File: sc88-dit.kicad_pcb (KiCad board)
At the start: 2 copper layers, 70 x 51 mm, 72 parts, among them J1 Conn_01x04_Male, J2 Conn_01x04_Male, J3 Conn_01x06_Male, J4 Conn_01x06_Male, U1 74LVC1G74, U2 AK4103A

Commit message: Added an oppai-sauce logo
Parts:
- added G***: LOGO, components:opppaisauce, B.Cu at (34.2, 115.0)

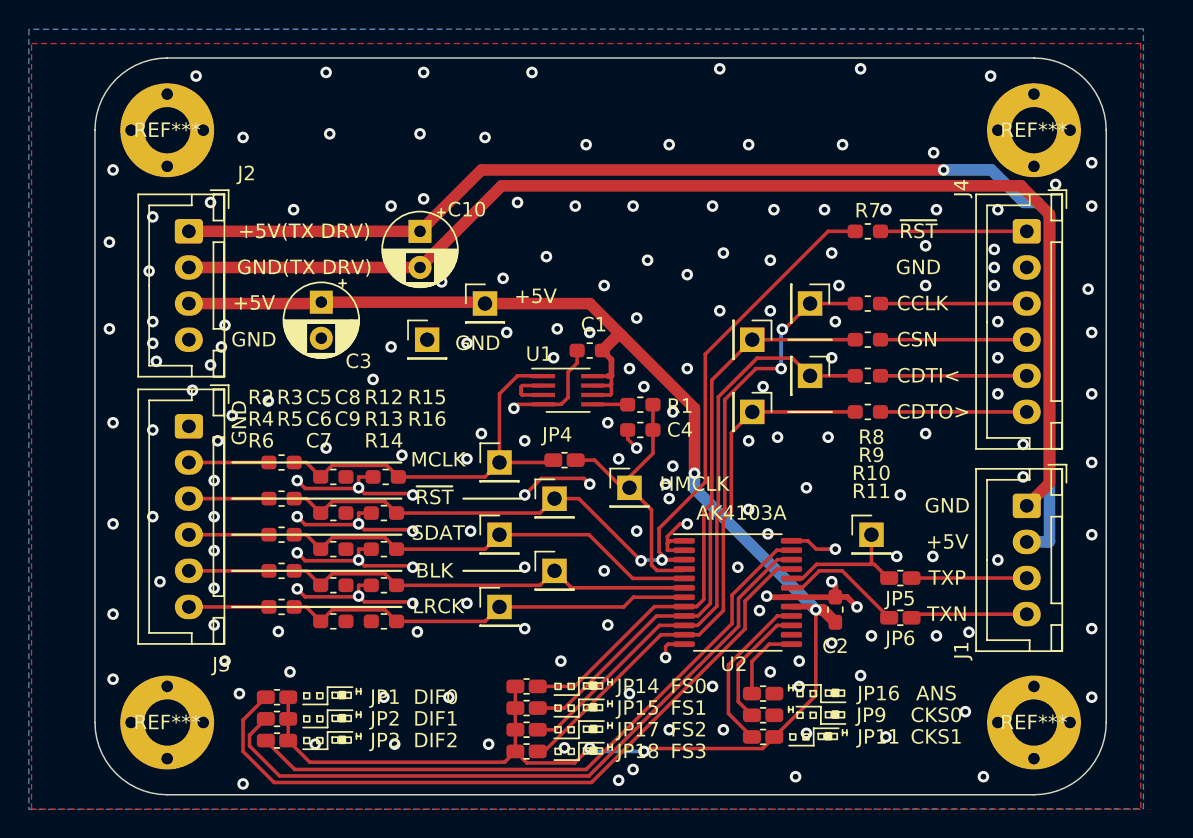
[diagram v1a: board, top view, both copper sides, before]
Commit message: To use right-angle connectors
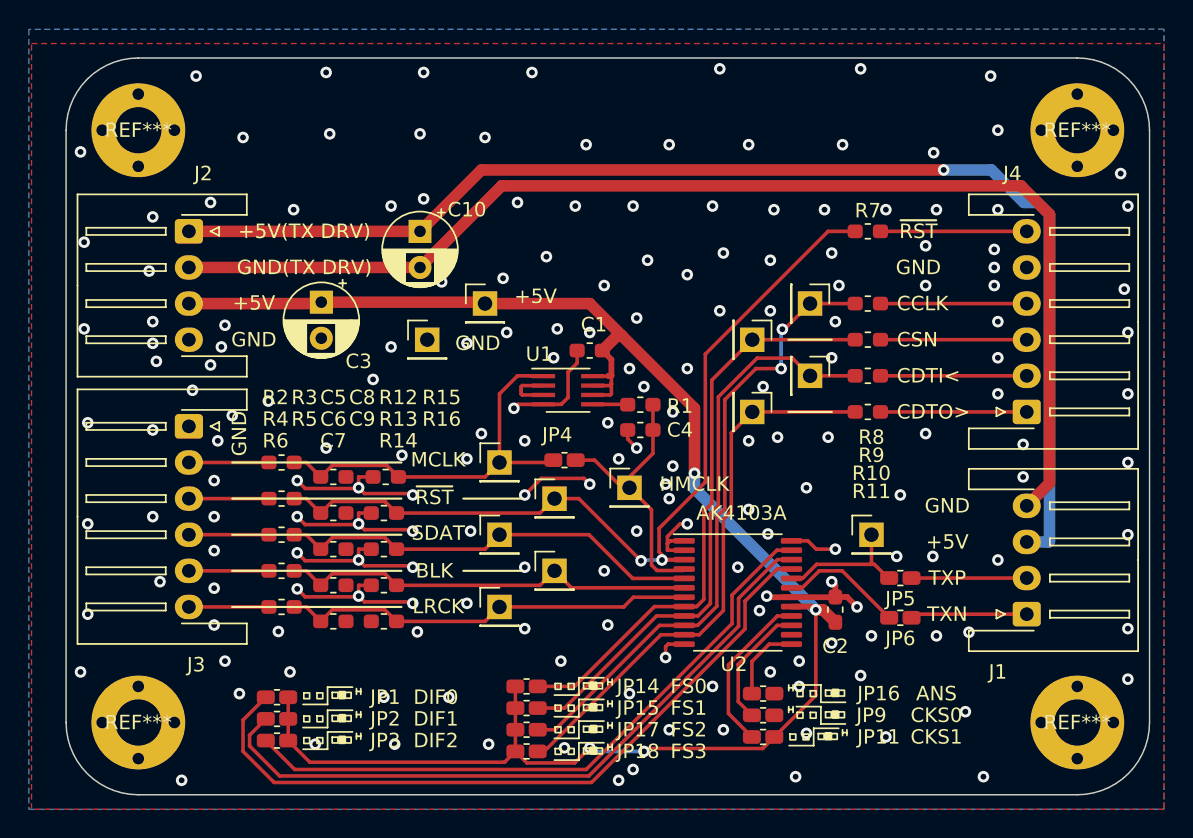
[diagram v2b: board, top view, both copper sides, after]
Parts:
- J1, J2: footprint Connector_JST:JST_XH_B4B-XH-A_1x04_P2.50mm_Vertical -> Connector_JST:JST_XH_S4B-XH-A-1_1x04_P2.50mm_Horizontal
- J3, J4: footprint Connector_JST:JST_XH_B6B-XH-A_1x06_P2.50mm_Vertical -> Connector_JST:JST_XH_S6B-XH-A-1_1x06_P2.50mm_Horizontal
- moved J4 12.5 mm to (81.5, 104.5), turned to 90 degrees
- moved J1 7.50 mm to (81.5, 118.5), turned to 90 degrees
- moved REF*** 3.00 mm to (85.0, 126.0)
- moved REF*** 3.00 mm to (85.0, 85.0)
- moved REF*** 2.00 mm to (20.0, 85.0)
- moved REF*** 2.00 mm to (20.0, 126.0)
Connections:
- J1 pad 1: /LEDK -> Net-(J1-Pad1)
- J1 pad 2: /LEDA -> Net-(J1-Pad2)
- J1 pad 3: Net-(J1-Pad3) -> /LEDA
- J1 pad 4: Net-(J1-Pad4) -> /LEDK
- J4 pad 2: GND -> Net-(J4-Pad2)
- J4 pad 5: Net-(J4-Pad5) -> GND
- JP5 pad 1: Net-(J1-Pad3) -> Net-(J1-Pad2)
- JP6 pad 1: Net-(J1-Pad4) -> Net-(J1-Pad1)
- R10 pad 2: Net-(J4-Pad5) -> Net-(J4-Pad2)
- R11 pad 2: Net-(J4-Pad6) -> Net-(J4-Pad1)
- R7 pad 2: Net-(J4-Pad1) -> Net-(J4-Pad6)
- R8 pad 2: Net-(J4-Pad3) -> Net-(J4-Pad4)
- R9 pad 2: Net-(J4-Pad4) -> Net-(J4-Pad3)
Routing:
- net Net-(J4-Pad5): track 10.1 -> 0.00 mm
- net Net-(J4-Pad2): track 0.00 -> 10.1 mm
- net Net-(J1-Pad4): track 8.08 -> 0.00 mm
- net Net-(J1-Pad1): track 0.00 -> 8.08 mm
- net Net-(J1-Pad3): track 7.97 -> 0.00 mm
- net Net-(J1-Pad2): track 0.00 -> 7.97 mm
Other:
- board size 70 x 51 mm -> 75 x 51 mm

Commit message: Refined VCC line
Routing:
- net +5V: track 123.1 -> 127.6 mm
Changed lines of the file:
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@@
   (general
     (thickness 1.6)
-    (drawings 51)
-    (tracks 517)
+    (drawings 52)
+    (tracks 521)
     (modules 73)
     (nets 37)
@@
     (tags "resistor handsolder")
     (attr smd)
-    (fp_text reference "R11" (at 0.25 5.5) (layer "F.SilkS")
+    (fp_text reference "R11" (at -0.15 3) (layer "F.SilkS")
       (effects (font (size 1 1) (thickness 0.15)))
     )
@@
     (tags "resistor handsolder")
     (attr smd)
-    (fp_text reference "R10" (at 0.25 6.75) (layer "F.SilkS")
+    (fp_text reference "R10" (at -0.15 4.15) (layer "F.SilkS")
       (effects (font (size 1 1) (thickness 0.15)))
     )
@@
     (tags "resistor handsolder")
     (attr smd)
-    (fp_text reference "R9" (at 0.25 8) (layer "F.SilkS")
+    (fp_text reference "R9" (at 0.05 -4.2) (layer "F.SilkS")
       (effects (font (size 1 1) (thickness 0.15)))
     )
@@
     (tags "resistor handsolder")
     (attr smd)
-    (fp_text reference "R8" (at 0.25 9.25) (layer "F.SilkS")
+    (fp_text reference "R8" (at 0.05 -3.3) (layer "F.SilkS")
       (effects (font (size 1 1) (thickness 0.15)))
     )
@@
     )
   )
+  (gr_text "TXP" (at 67.65 111.65) (layer "F.SilkS")
+    (effects (font (size 1 1) (thickness 0.15)))
+  )
   (gr_text "GND" (at 27 106 90) (layer "F.SilkS")
     (effects (font (size 1 1) (thickness 0.15)))
@@
     (effects (font (size 1 1) (thickness 0.15)))
   )
+  (via (at 67.7 121.6) (size 0.8) (drill 0.4) (layers "F.Cu" "B.Cu") (net 2))
+  (via (at 65.45 121.75) (size 0.8) (drill 0.4) (layers "F.Cu" "B.Cu") (net 2))
+  (segment (start 68.25032 119.44968) (end 66.55 121.15) (width 0.25) (layer "F.Cu") (net 3))
+  (segment (start 68.25032 119.058874) (end 68.25032 119.44968) (width 0.25) (layer "F.Cu") (net 3))
+  (segment (start 66.55 124.475) (end 64.025 127) (width 0.25) (layer "F.Cu") (net 3))
+  (segment (start 66.55 121.15) (end 66.55 124.475) (width 0.25) (layer "F.Cu") (net 3))
+  (segment (start 65.2125 117.975) (end 66.375 117.975) (width 0.4) (layer "F.Cu") (net 3))
+  (segment (start 66.375 117.975) (end 67.05 118.65) (width 0.4) (layer "F.Cu") (net 3))
+  (segment (start 67.05 118.65) (end 67.458874 119.058874) (width 0.4) (layer "F.Cu") (net 3))
+  (segment (start 67.458874 119.058874) (end 68.25032 119.058874) (width 0.4) (layer "F.Cu") (net 3))
+  (segment (start 67.2 119.1) (end 69.6 119.1) (width 0.8) (layer "B.Cu") (net 3))
+  (segment (start 69.558874 119.058874) (end 69.6 119.1) (width 0.8) (layer "F.Cu") (net 3))
+  (segment (start 68.25032 119.058874) (end 69.558874 119.058874) (width 0.8) (layer "F.Cu") (net 3))
+  (segment (start 58.5 110.4) (end 67.2 119.1) (width 0.8) (layer "B.Cu") (net 3))
+  (segment (start 58.5 108.75) (end 58.5 110.4) (width 0.8) (layer "B.Cu") (net 3))
+  (via (at 69.6 119.1) (size 0.8) (drill 0.4) (layers "F.Cu" "B.Cu") (net 3))
   (via (at 62.25 111.25) (size 0.8) (drill 0.4) (layers "F.Cu" "B.Cu") (net 2))
   (via (at 61.5 115.25) (size 0.8) (drill 0.4) (layers "F.Cu" "B.Cu") (net 2))
-  (segment (start 66.6 117.9) (end 66.9 118.2) (width 0.8) (layer "B.Cu") (net 3))
-  (segment (start 58.5 108.75) (end 58.5 109.8) (width 0.8) (layer "B.Cu") (net 3))
-  (segment (start 58.5 109.8) (end 66.6 117.9) (width 0.8) (layer "B.Cu") (net 3))
   (via (at 63.582059 112.945294) (size 0.8) (drill 0.4) (layers "F.Cu" "B.Cu") (net 2))
   (via (at 38.25 107.5) (size 0.8) (drill 0.4) (layers "F.Cu" "B.Cu") (net 2))
@@
   (segment (start 68.25032 116.50032) (end 68 116.25) (width 0.4) (layer "F.Cu") (net 2))
   (via (at 68 116.25) (size 0.8) (drill 0.4) (layers "F.Cu" "B.Cu") (net 2))
-  (via (at 68 120.5) (size 0.8) (drill 0.4) (layers "F.Cu" "B.Cu") (net 2))
   (segment (start 69.058874 117.308874) (end 69.75 118) (width 0.4) (layer "F.Cu") (net 2))
   (segment (start 65.2125 117.325) (end 68.234194 117.325) (width 0.4) (layer "F.Cu") (net 2))
   (segment (start 68.25032 117.308874) (end 69.058874 117.308874) (width 0.4) (layer "F.Cu") (net 2))
-  (segment (start 67.391446 118.2) (end 68.25032 119.058874) (width 0.8) (layer "F.Cu") (net 3))
-  (segment (start 66.9 118.2) (end 67.391446 118.2) (width 0.8) (layer "F.Cu") (net 3))
   (segment (start 68.234194 117.325) (end 68.25032 117.308874) (width 0.4) (layer "F.Cu") (net 2))
   (via (at 58 95) (size 0.8) (drill 0.4) (layers "F.Cu" "B.Cu") (net 2))
@@
   (via (at 59.75 123.5) (size 0.8) (drill 0.4) (layers "F.Cu" "B.Cu") (net 2))
   (via (at 65.75 123.5) (size 0.8) (drill 0.4) (layers "F.Cu" "B.Cu") (net 2))
-  (via (at 65.75 121.75) (size 0.8) (drill 0.4) (layers "F.Cu" "B.Cu") (net 2))
   (via (at 63.75 122.5) (size 0.8) (drill 0.4) (layers "F.Cu" "B.Cu") (net 2))
   (via (at 54.25 129.25) (size 0.8) (drill 0.4) (layers "F.Cu" "B.Cu") (net 2))
@@
   (via (at 55 128) (size 0.8) (drill 0.4) (layers "F.Cu" "B.Cu") (net 3))
   (segment (start 63.22499 127.80001) (end 55.19999 127.80001) (width 0.25) (layer "F.Cu") (net 3))
-  (segment (start 66.9 118.2) (end 66.9 124.125) (width 0.25) (layer "F.Cu") (net 3))
-  (segment (start 66.9 124.125) (end 64.025 127) (width 0.25) (layer "F.Cu") (net 3))
   (segment (start 71.375 97) (end 81.5 97) (width 0.25) (layer "F.Cu") (net 23))
   (segment (start 71.375 99.5) (end 81.5 99.5) (width 0.25) (layer "F.Cu") (net 24))
@@
   (segment (start 31.625 108) (end 32.625 109) (width 0.25) (layer "F.Cu") (net 8))
   (segment (start 23.5 108) (end 29.04 108) (width 0.25) (layer "F.Cu") (net 21))
-  (segment (start 65.2125 117.975) (end 66.675 117.975) (width 0.4) (layer "F.Cu") (net 3))
-  (segment (start 66.675 117.975) (end 66.9 118.2) (width 0.4) (layer "F.Cu") (net 3))
-  (via (at 66.9 118.2) (size 0.8) (drill 0.4) (layers "F.Cu" "B.Cu") (net 3))
   (segment (start 32.667763 96.902208) (end 43.902208 96.902208) (width 0.8) (layer "F.Cu") (net 3))
   (segment (start 43.902208 96.902208) (end 44 97) (width 0.8) (layer "F.Cu") (net 3))

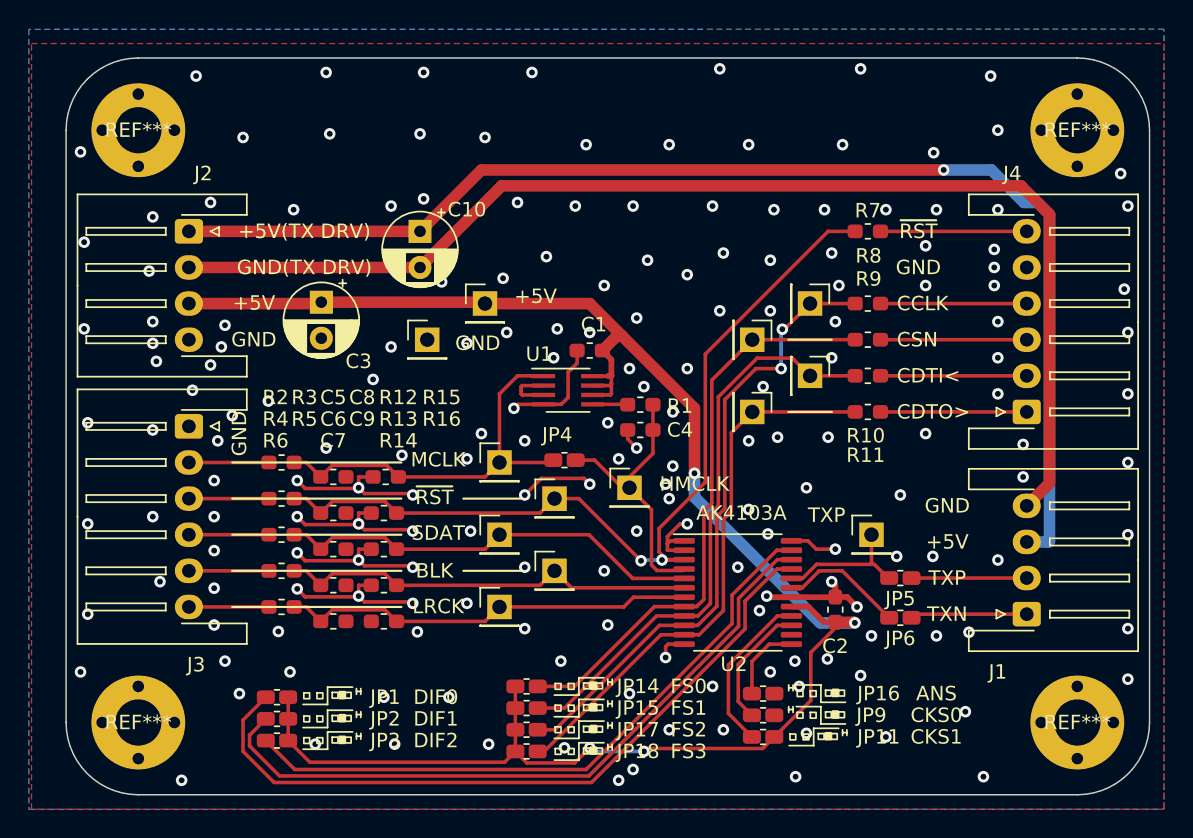
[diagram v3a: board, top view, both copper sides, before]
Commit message: Added NB3N511 clock multiplier to make MCLK from BCLK
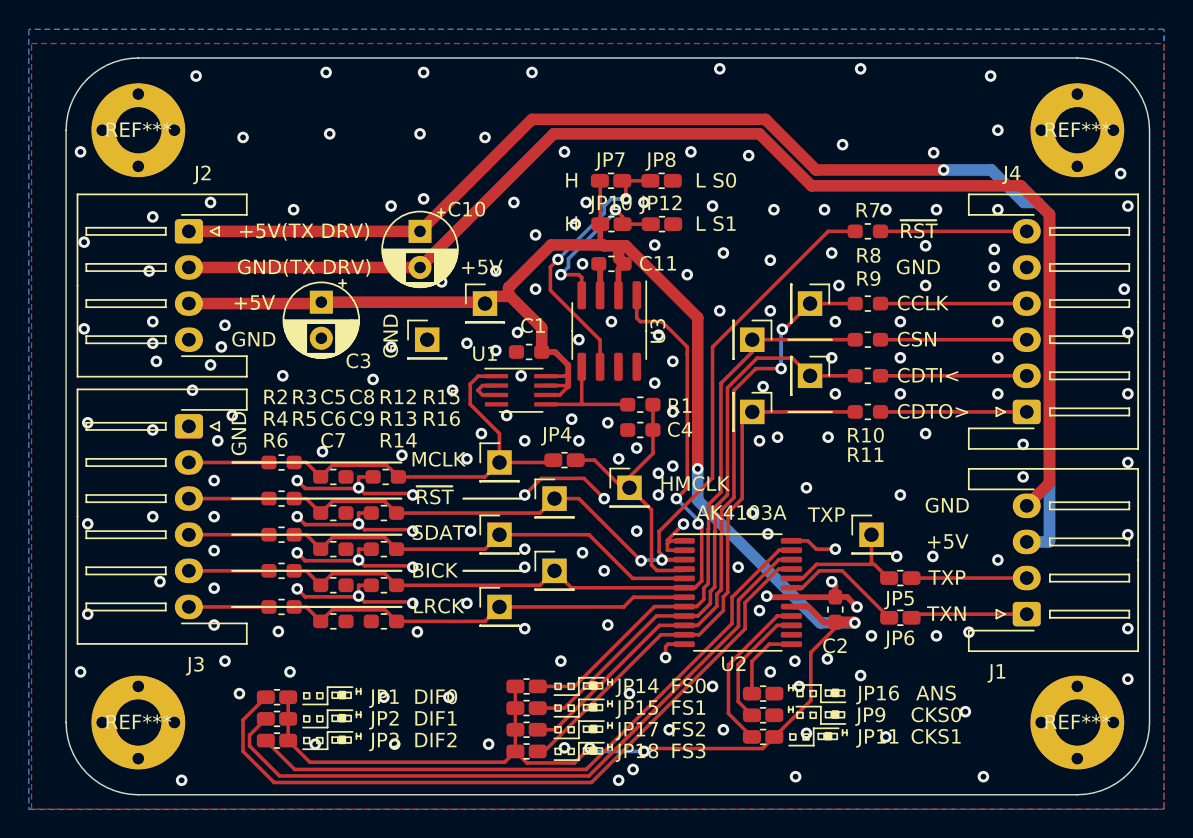
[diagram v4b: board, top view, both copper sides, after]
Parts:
- added C11: 0.1u/35V, Capacitor_SMD:C_0603_1608Metric_Pad1.05x0.95mm_HandSolder, F.Cu at (52.8, 94.2)
- added JP10: Jumper_NO_Small, components:R_0603_1608Metric_SolderJumperCompatible, F.Cu at (52.8, 91.5)
- added JP12: Jumper_NO_Small, components:R_0603_1608Metric_SolderJumperCompatible, F.Cu at (56.2, 91.5)
- added JP7: Jumper_NO_Small, components:R_0603_1608Metric_SolderJumperCompatible, F.Cu at (52.7, 88.5)
- added JP8: Jumper_NO_Small, components:R_0603_1608Metric_SolderJumperCompatible, F.Cu at (56.2, 88.5)
- added U3: NB3N511, Package_SO:SOIC-8_3.9x4.9mm_P1.27mm, F.Cu at (52.6, 98.9)
- moved C1 4.20 mm to (47.0, 100.3)
- moved U1 3.25 mm to (46.5, 103.0)
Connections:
- net /BLK renamed /BICK
- net Net-(R1-Pad1) renamed /MULDIV_CLK
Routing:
- net /BICK: track 29.0 -> 53.5 mm, vias 0 -> 2
- net +5V: track 127.6 -> 147.0 mm
- net /I511_S0: track 0.00 -> 19.1 mm, vias 0 -> 2
- net /I511_S1: track 0.00 -> 12.0 mm, vias 0 -> 2
- net /MULDIV_CLK: track 2.44 -> 8.30 mm
- net GND: track 72.9 -> 67.2 mm, vias 188 -> 199
- net /LEDK: track 83.6 -> 86.5 mm
- net /LEDA: track 86.8 -> 89.7 mm
- net Net-(U1-Pad2): track 3.66 -> 2.87 mm
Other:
- board text added: "BICK"
- board text added: "H"
- board text added: "L S0"
- board text added: "L S1"
- board text removed: "BLK"

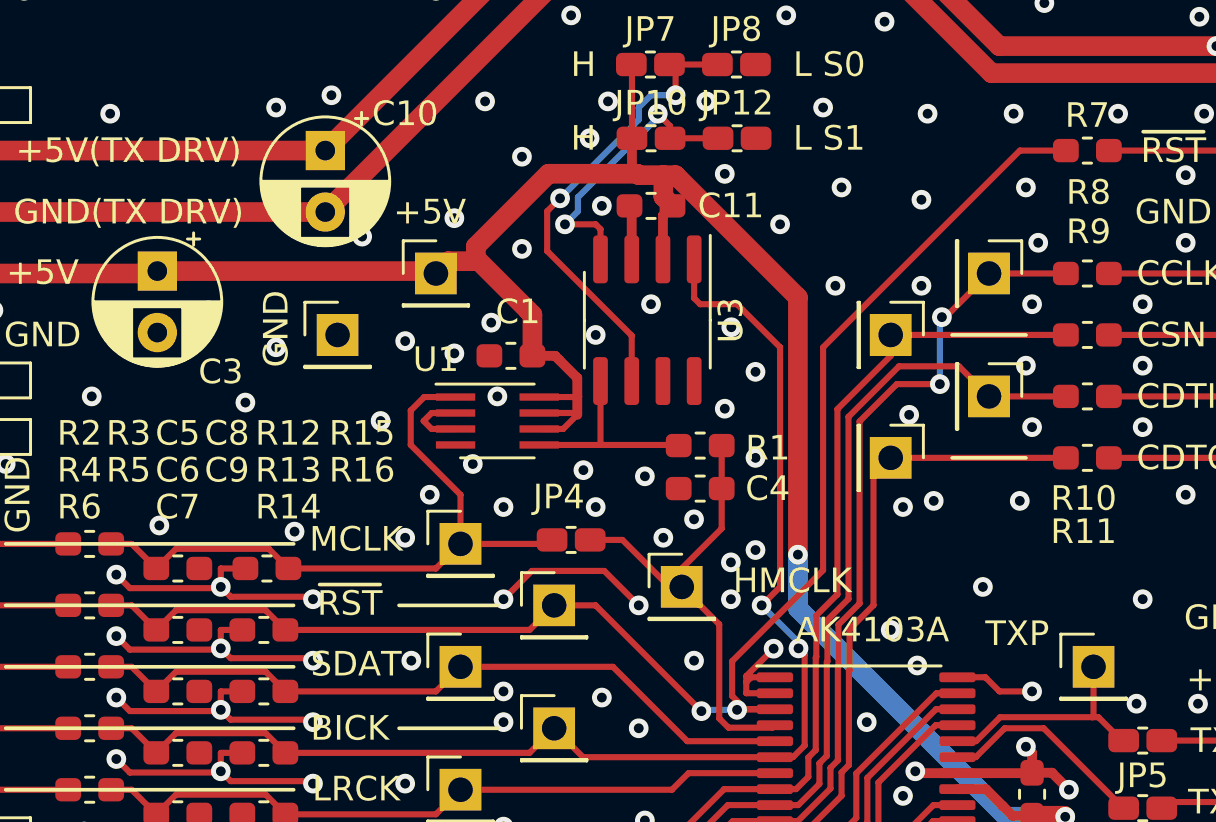
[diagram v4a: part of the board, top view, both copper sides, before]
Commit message: To be able to select multiplier's input from MCLK and BICK
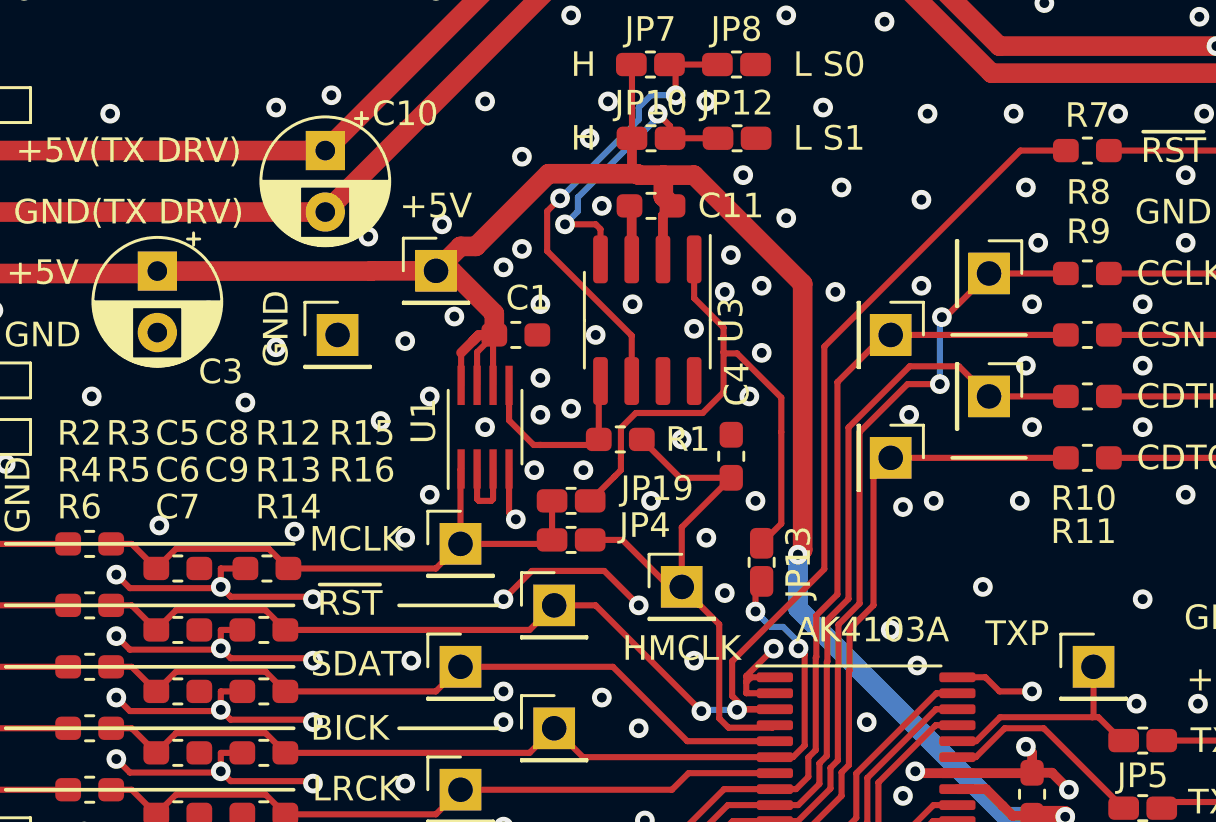
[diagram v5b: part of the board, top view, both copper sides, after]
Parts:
- added JP13: Jumper_NO_Small, components:R_0603_1608Metric_SolderJumperCompatible, F.Cu at (57.2, 108.8)
- added JP19: Jumper_NO_Small, components:R_0603_1608Metric_SolderJumperCompatible, F.Cu at (49.5, 106.2)
- moved R1 3.26 mm to (51.5, 103.8)
- moved C4 1.82 mm to (56.0, 104.4), turned to 90 degrees
- moved C1 0.87 mm to (47.2, 99.5), turned to 0 degrees
- moved U1 0.56 mm to (46.0, 103.2), turned to 90 degrees
- moved TP2 0.11 mm to (44.0, 96.9)
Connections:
- U3 pad 1: /BICK -> Net-(JP13-Pad2)
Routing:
- net Net-(JP13-Pad2): track 0.00 -> 23.5 mm
- net /BICK: track 53.5 -> 38.3 mm
- net /MCLK: track 27.8 -> 24.1 mm
- net /HALF_MCLK: track 19.4 -> 22.5 mm
- net GND: track 67.2 -> 69.4 mm, vias 199 -> 204
- net +5V: track 147.0 -> 145.3 mm

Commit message: Added a description text on the board
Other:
- board text added: "I2S to S/PDIF converter board Rev. 1.0"
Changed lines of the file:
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@@
   (general
     (thickness 1.6)
-    (drawings 56)
+    (drawings 57)
     (tracks 622)
     (modules 81)
@@
     )
   )
+  (gr_text "I2S to S/PDIF converter board\nRev. 1.0" (at 29.25 84.5) (layer "F.SilkS")
+    (effects (font (size 2 2) (thickness 0.3)) (justify left))
+  )
   (gr_text "+5V" (at 44 94.25) (layer "F.SilkS")
